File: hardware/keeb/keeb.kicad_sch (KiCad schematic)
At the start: 162 parts, among them J101 AVR-ISP-6, J102 USB_C_Receptacle_USB2.0, SW101 SW_Push, SW102 SW_Push, SW103 SW_Push, SW104 SW_Push, SW105 SW_Push, SW106 SW_Push, SW107 SW_Push, SW108 SW_Push, SW109 SW_Push, SW110 SW_Push, SW111 SW_Push, SW112 SW_Push, SW113 SW_Push, SW114 SW_Push, SW115 SW_Push, SW116 SW_Push, SW117 SW_Push, SW118 SW_Push, SW119 SW_Push, SW120 SW_Push, SW121 SW_Push, SW122 SW_Push, SW123 SW_Push, SW124 SW_Push, SW125 SW_Push, SW126 SW_Push, SW127 SW_Push, SW128 SW_Push, SW129 SW_Push, SW130 SW_Push, SW131 SW_Push, SW132 SW_Push, SW133 SW_Push, SW134 SW_Push, SW135 SW_Push, SW136 SW_Push, SW137 SW_Push, SW138 SW_Push, SW139 SW_Push, SW140 SW_Push, SW141 SW_Push, SW142 SW_Push, SW143 SW_Push, SW144 SW_Push, SW145 SW_Push, SW146 SW_Push, SW147 SW_Push, SW148 SW_Push, SW149 SW_Push, SW150 SW_Push, SW151 SW_Push, SW152 SW_Push, SW153 SW_Push, SW154 SW_Push, SW155 SW_Push, SW156 SW_Push, SW157 SW_Push, SW158 SW_Push, SW159 SW_Push, SW160 SW_Push, SW161 SW_Push, SW162 SW_Push, SW163 SW_Push, SW164 SW_Push, SW165 SW_Push, SW166 SW_Push, SW167 SW_Push, U101 TPD2S017, U102 ATmega32U4-MU, Y101 16Mhz

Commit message: final parts and LCSC bom
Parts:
- C101, C107: LCSC Link https://datasheet.lcsc.com/lcsc/1810261812_Samsung-Electro-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 -> https://lcsc.com/product-detail/Multilayer-Ceramic-Capacito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
- R107, R108: value 22 -> 22R; LCSC Link https://www.lcsc.com/product-detail/Chip-Resistor---Surface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 -> https://lcsc.com/product-detail/Chip-Resistor---Surface-Mou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
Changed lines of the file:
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@@
       (effects (font (size 1.27 1.27)) hide)
     )
-    (property "Datasheet" "https://www.lcsc.com/product-detail/Multilayer-Ceramic-Capacitors-MLCC---SMD-SMT_Samsung-Electro-Mechanics-Samsung-Electro-Mechanics-CL10A105KB8NNNC_C15849.html" (at 116.84 31.75 0)
+    (property "Datasheet" "https://datasheet.lcsc.com/lcsc/1810261812_Samsung-Electro-Mechanics-CL10A105KB8NNNC_C15849.pdf" (at 116.84 31.75 0)
       (effects (font (size 1.27 1.27)) hide)
     )
@@
       (effects (font (size 1.27 1.27)) hide)
     )
-    (property "LCSC Link" "https://datasheet.lcsc.com/lcsc/1810261812_Samsung-Electro-Mechanics-CL10A105KB8NNNC_C15849.pdf" (at 116.84 31.75 0)
+    (property "LCSC Link" "https://lcsc.com/product-detail/Multilayer-Ceramic-Capacitors-MLCC---SMD-SMT_Samsung-Electro-Mechanics-Samsung-Electro-Mechanics-CL10A105KB8NNNC_C15849.html" (at 116.84 31.75 0)
       (effects (font (size 1.27 1.27)) hide)
     )
@@
       (effects (font (size 1.27 1.27)))
     )
-    (property "Value" "22" (at 201.93 94.615 90)
+    (property "Value" "22R" (at 201.93 94.615 90)
       (effects (font (size 1.27 1.27)))
     )
@@
       (effects (font (size 1.27 1.27)) hide)
     )
-    (property "LCSC Link" "https://www.lcsc.com/product-detail/Chip-Resistor---Surface-Mount_UNI-ROYALUniroyal-Elec-UNI-ROYALUniroyal-Elec-0402WGF220JTCE_C25092.html" (at 201.93 96.52 0)
+    (property "LCSC Link" "https://lcsc.com/product-detail/Chip-Resistor---Surface-Mount_UNI-ROYALUniroyal-Elec-UNI-ROYALUniroyal-Elec-0402WGF220JTCE_C25092.html" (at 201.93 96.52 0)
       (effects (font (size 1.27 1.27)) hide)
     )
@@
       (effects (font (size 1.27 1.27)))
     )
-    (property "Value" "22" (at 201.93 100.965 90)
+    (property "Value" "22R" (at 201.93 100.965 90)
       (effects (font (size 1.27 1.27)))
     )
@@
       (effects (font (size 1.27 1.27)) hide)
     )
-    (property "LCSC Link" "https://www.lcsc.com/product-detail/Chip-Resistor---Surface-Mount_UNI-ROYALUniroyal-Elec-UNI-ROYALUniroyal-Elec-0402WGF220JTCE_C25092.html" (at 201.93 99.06 0)
+    (property "LCSC Link" "https://lcsc.com/product-detail/Chip-Resistor---Surface-Mount_UNI-ROYALUniroyal-Elec-UNI-ROYALUniroyal-Elec-0402WGF220JTCE_C25092.html" (at 201.93 99.06 0)
       (effects (font (size 1.27 1.27)) hide)
     )
@@
     )
     (property "Datasheet" " ~" (at 106.045 91.44 0)
-      (effects (font (size 1.27 1.27)) hide)
-    )
-    (property "man#" "" (at 138.43 77.47 0)
       (effects (font (size 1.27 1.27)) hide)
     )
@@
       (effects (font (size 1.27 1.27)) hide)
     )
-    (property "Datasheet" "https://www.lcsc.com/product-detail/Multilayer-Ceramic-Capacitors-MLCC---SMD-SMT_Samsung-Electro-Mechanics-Samsung-Electro-Mechanics-CL10A105KB8NNNC_C15849.html" (at 207.01 107.95 0)
+    (property "Datasheet" "https://datasheet.lcsc.com/lcsc/1810261812_Samsung-Electro-Mechanics-CL10A105KB8NNNC_C15849.pdf" (at 207.01 107.95 0)
       (effects (font (size 1.27 1.27)) hide)
     )
@@
       (effects (font (size 1.27 1.27)) hide)
     )
-    (property "LCSC Link" "https://datasheet.lcsc.com/lcsc/1810261812_Samsung-Electro-Mechanics-CL10A105KB8NNNC_C15849.pdf" (at 207.01 107.95 0)
-      (effects (font (size 1.27 1.27)) hide)
-    )
+    (property "LCSC Link" "https://lcsc.com/product-detail/Multilayer-Ceramic-Capacitors-MLCC---SMD-SMT_Samsung-Electro-Mechanics-Samsung-Electro-Mechanics-CL10A105KB8NNNC_C15849.html" (at 207.01 107.95 0)
+      (effects (font (size 1.27 1.27)) hide)
+    )

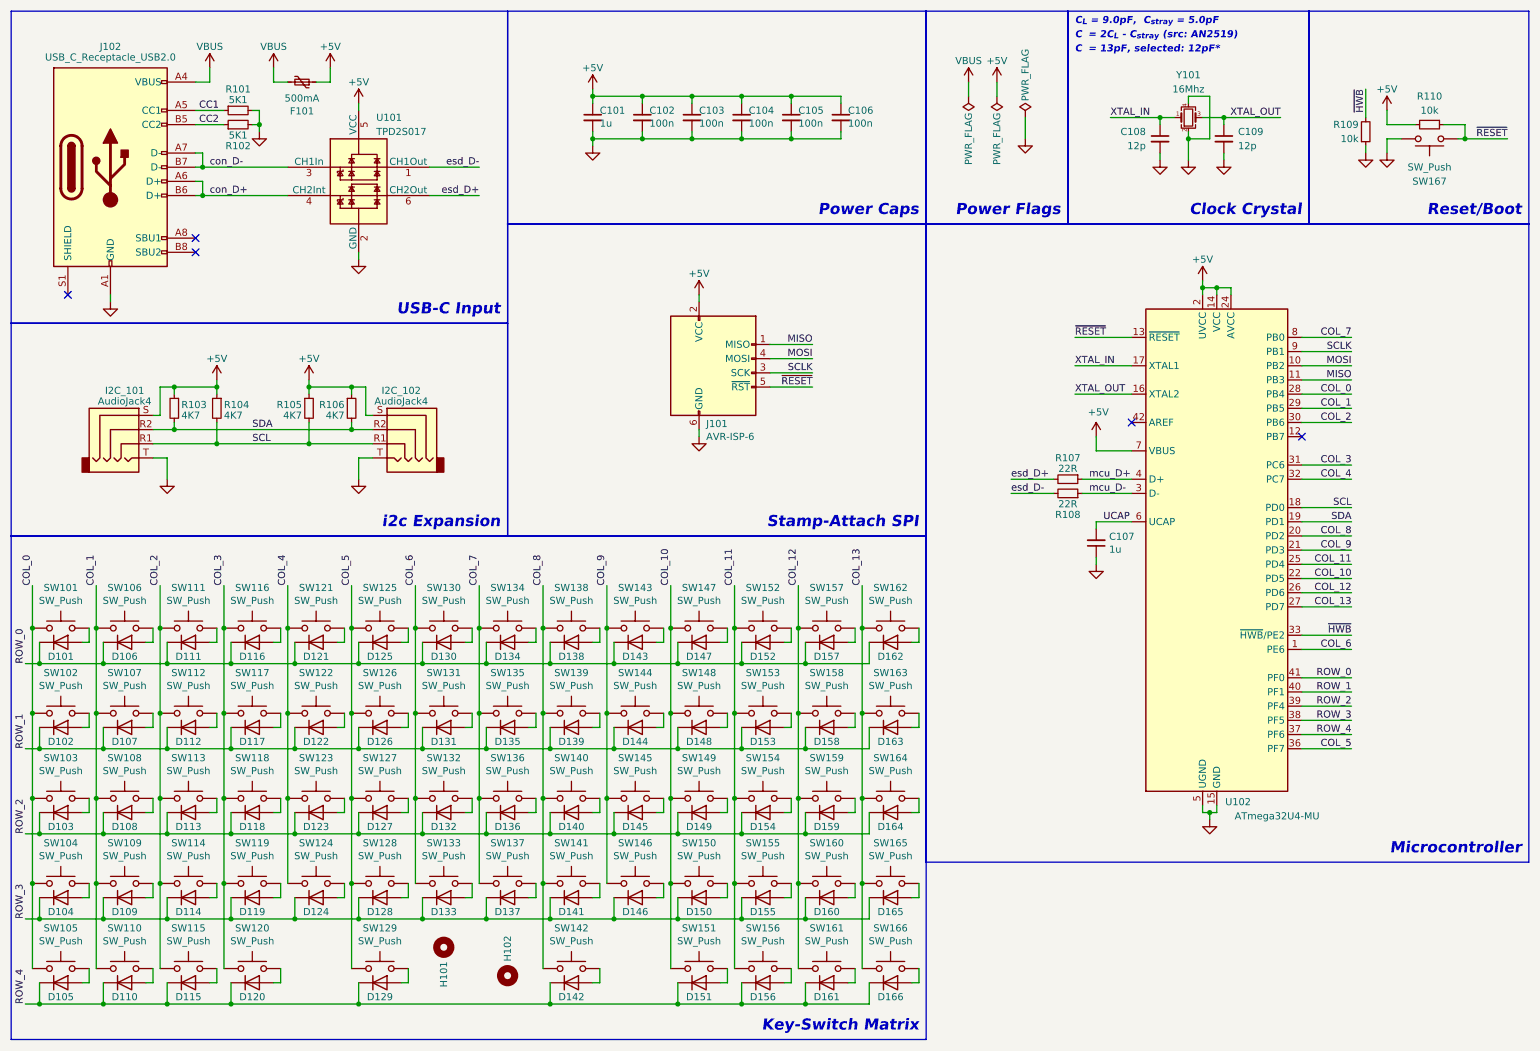
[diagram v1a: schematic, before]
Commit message: schem info text, and README updated
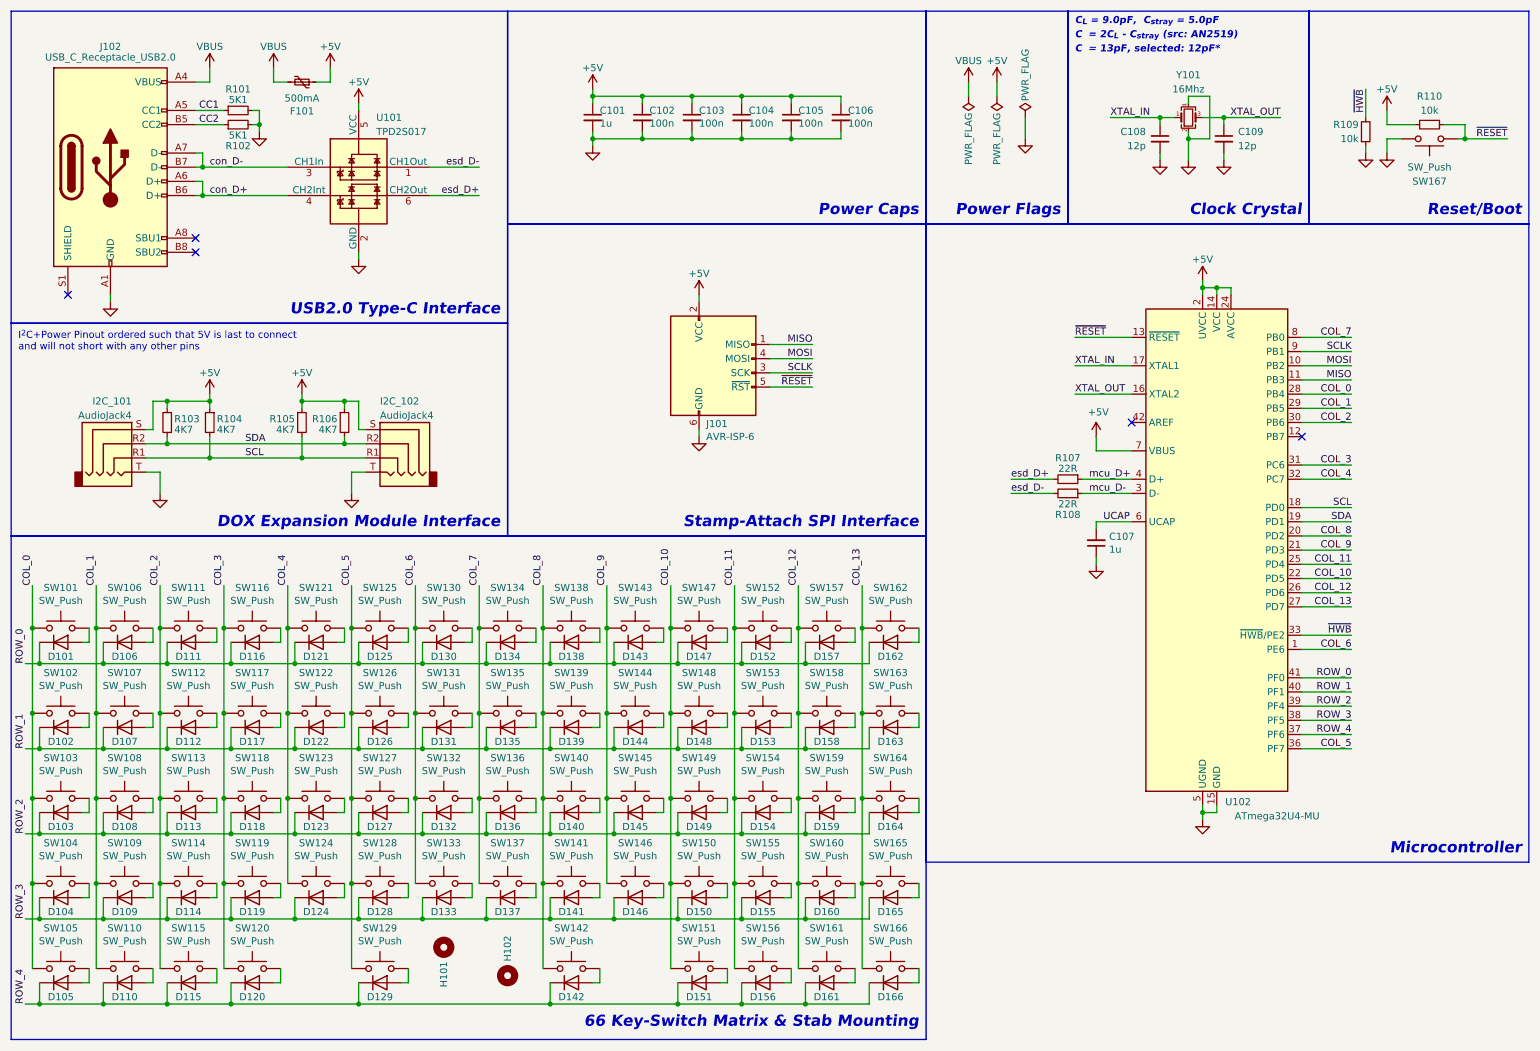
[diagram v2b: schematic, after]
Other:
- note added: "66 Key-Switch Matrix & Stab Mounting"
- note added: "DOX Expansion Module Interface"
- note added: "I^{2}C+Power Pinout ordered such that 5V is last to connect and will not short with any other pins"
- note added: "Stamp-Attach SPI Interface"
- note added: "USB2.0 Type-C Interface"
- note removed: "Key-Switch Matrix"
- note removed: "Stamp-Attach SPI"
- note removed: "USB-C Input"
- note removed: "i2c Expansion"
- moved on the sheet: I2C_101, I2C_102, R103, R104, R105, R106
